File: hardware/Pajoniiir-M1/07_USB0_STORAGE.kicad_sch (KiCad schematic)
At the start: 7 parts

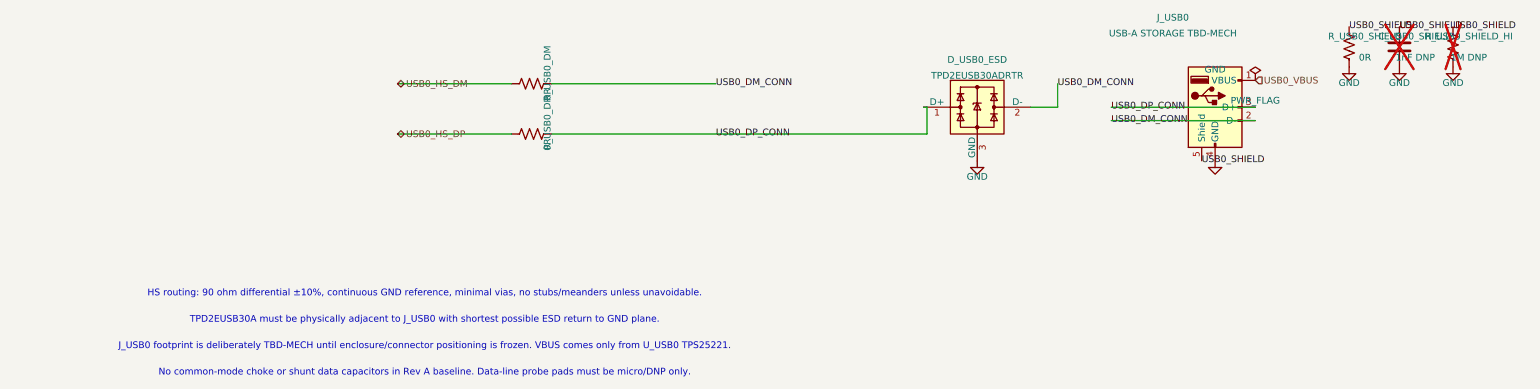
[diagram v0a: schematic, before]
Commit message: hardware: normalize schematic reference designators
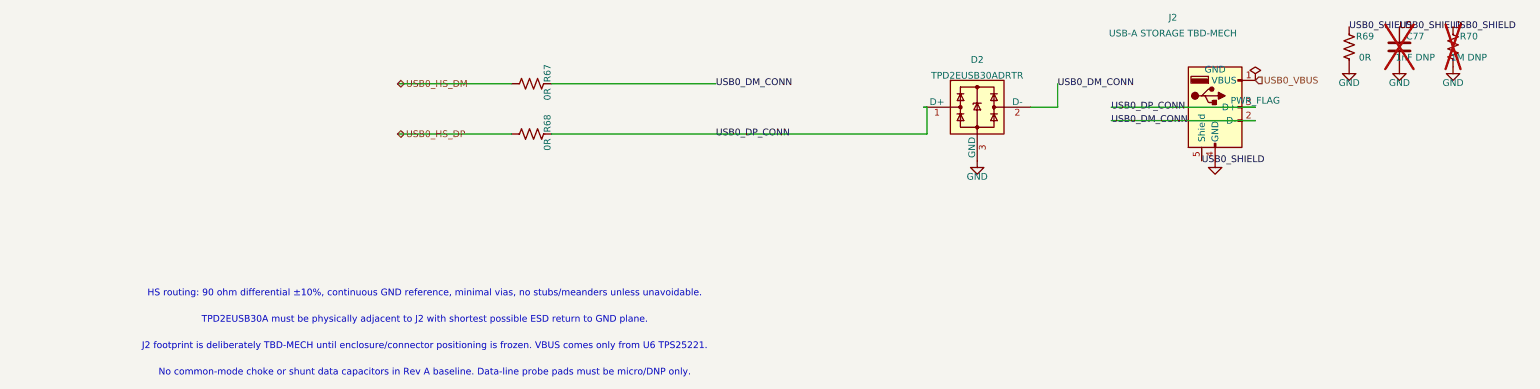
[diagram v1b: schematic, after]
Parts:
- renumbered C_USB0_SHIELD to C77, D_USB0_ESD to D2, J_USB0 to J2, R_USB0_DM to R67, R_USB0_DP to R68, R_USB0_SHIELD to R69, R_USB0_SHIELD_HI to R70
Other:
- note added: "J2 footprint is deliberately TBD-MECH until enclosure/connector positioning is frozen. VBUS comes only from U6 TPS25221."
- note added: "TPD2EUSB30A must be physically adjacent to J2 with shortest possible ESD return to GND plane."
- note removed: "J_USB0 footprint is deliberately TBD-MECH until enclosure/connector positioning is frozen. VBUS comes only from U_USB0 TPS25221."
- note removed: "TPD2EUSB30A must be physically adjacent to J_USB0 with shortest possible ESD return to GND plane."
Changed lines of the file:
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@@
     (lib_id "Device:R_US") (at 55.245 55.245 90) (unit 1)
     (exclude_from_sim no) (in_bom yes) (on_board yes) (dnp no)
-    (property "Reference" "R_USB0_DM" (at 58.245 53.245 0) (effects (font (size 1.27 1.27))))
+    (property "Reference" "R67" (at 58.245 53.245 0) (effects (font (size 1.27 1.27))))
     (property "Value" "0R" (at 58.245 57.245 0) (effects (font (size 1.27 1.27))))
     (property "Footprint" "Resistor_SMD:R_0402_1005Metric" (at 55.245 55.245 0) (effects (font (size 1.27 1.27)) (hide yes)))
     (property "Datasheet" "~" (at 55.245 55.245 0) (effects (font (size 1.27 1.27)) (hide yes)))
     (pin "1") (pin "2")
-    (instances (project "Pajoniiir-M1" (path "/2c8dd352-b7b8-4d9e-8f93-5dd43be2a100/31000007-6b2a-4a3a-8c91-000000000007" (reference "R_USB0_DM") (unit 1))))
+    (instances (project "Pajoniiir-M1" (path "/2c8dd352-b7b8-4d9e-8f93-5dd43be2a100/31000007-6b2a-4a3a-8c91-000000000007" (reference "R67") (unit 1))))
   )
   (wire (pts (xy 29.845 55.245) (xy 51.435 55.245)) (stroke (width 0) (type default)))
@@
     (lib_id "Device:R_US") (at 55.245 64.77 90) (unit 1)
     (exclude_from_sim no) (in_bom yes) (on_board yes) (dnp no)
-    (property "Reference" "R_USB0_DP" (at 58.245 62.77 0) (effects (font (size 1.27 1.27))))
+    (property "Reference" "R68" (at 58.245 62.77 0) (effects (font (size 1.27 1.27))))
     (property "Value" "0R" (at 58.245 66.77 0) (effects (font (size 1.27 1.27))))
     (property "Footprint" "Resistor_SMD:R_0402_1005Metric" (at 55.245 64.77 0) (effects (font (size 1.27 1.27)) (hide yes)))
     (property "Datasheet" "~" (at 55.245 64.77 0) (effects (font (size 1.27 1.27)) (hide yes)))
     (pin "1") (pin "2")
-    (instances (project "Pajoniiir-M1" (path "/2c8dd352-b7b8-4d9e-8f93-5dd43be2a100/31000007-6b2a-4a3a-8c91-000000000007" (reference "R_USB0_DP") (unit 1))))
+    (instances (project "Pajoniiir-M1" (path "/2c8dd352-b7b8-4d9e-8f93-5dd43be2a100/31000007-6b2a-4a3a-8c91-000000000007" (reference "R68") (unit 1))))
   )
   (wire (pts (xy 29.845 64.77) (xy 51.435 64.77)) (stroke (width 0) (type default)))
@@
     (lib_id "Power_Protection:TPD2EUSB30A") (at 139.7 59.69 0) (unit 1)
     (exclude_from_sim no) (in_bom yes) (on_board yes) (dnp no)
-    (property "Reference" "D_USB0_ESD" (at 139.7 50.69 0) (effects (font (size 1.27 1.27))))
+    (property "Reference" "D2" (at 139.7 50.69 0) (effects (font (size 1.27 1.27))))
     (property "Value" "TPD2EUSB30ADRTR" (at 139.7 53.69 0) (effects (font (size 1.27 1.27))))
     (property "Footprint" "Package_TO_SOT_SMD:Texas_DRT-3" (at 139.7 59.69 0) (effects (font (size 1.27 1.27)) (hide yes)))
     (property "Datasheet" "https://www.ti.com/lit/ds/symlink/tpd2eusb30a.pdf" (at 139.7 59.69 0) (effects (font (size 1.27 1.27)) (hide yes)))
     (pin "1") (pin "2") (pin "3")
-    (instances (project "Pajoniiir-M1" (path "/2c8dd352-b7b8-4d9e-8f93-5dd43be2a100/31000007-6b2a-4a3a-8c91-000000000007" (reference "D_USB0_ESD") (unit 1))))
+    (instances (project "Pajoniiir-M1" (path "/2c8dd352-b7b8-4d9e-8f93-5dd43be2a100/31000007-6b2a-4a3a-8c91-000000000007" (reference "D2") (unit 1))))
   )
   (wire (pts (xy 130.175 64.77) (xy 130.175 59.69)) (stroke (width 0) (type default)))
@@
     (lib_id "Connector:USB_A") (at 184.785 59.69 0) (unit 1)
     (exclude_from_sim no) (in_bom yes) (on_board yes) (dnp no)
-    (property "Reference" "J_USB0" (at 176.785 42.69 0) (effects (font (size 1.27 1.27))))
+    (property "Reference" "J2" (at 176.785 42.69 0) (effects (font (size 1.27 1.27))))
     (property "Value" "USB-A STORAGE TBD-MECH" (at 176.785 45.69 0) (effects (font (size 1.27 1.27))))
     (property "Footprint" "" (at 184.785 59.69 0) (effects (font (size 1.27 1.27)) (hide yes)))
     (property "Datasheet" "~" (at 184.785 59.69 0) (effects (font (size 1.27 1.27)) (hide yes)))
     (pin "1") (pin "2") (pin "3") (pin "4") (pin "5")
-    (instances (project "Pajoniiir-M1" (path "/2c8dd352-b7b8-4d9e-8f93-5dd43be2a100/31000007-6b2a-4a3a-8c91-000000000007" (reference "J_USB0") (unit 1))))
+    (instances (project "Pajoniiir-M1" (path "/2c8dd352-b7b8-4d9e-8f93-5dd43be2a100/31000007-6b2a-4a3a-8c91-000000000007" (reference "J2") (unit 1))))
   )
   (hierarchical_label "USB0_VBUS" (shape input) (at 192.405 54.61 0) (effects (font (size 1.27 1.27))))
@@
     (lib_id "Device:R_US") (at 210.185 48.26 0) (unit 1)
     (exclude_from_sim no) (in_bom yes) (on_board yes) (dnp no)
-    (property "Reference" "R_USB0_SHIELD" (at 213.185 46.26 0) (effects (font (size 1.27 1.27))))
+    (property "Reference" "R69" (at 213.185 46.26 0) (effects (font (size 1.27 1.27))))
     (property "Value" "0R" (at 213.185 50.26 0) (effects (font (size 1.27 1.27))))
     (property "Footprint" "Resistor_SMD:R_0603_1608Metric" (at 210.185 48.26 0) (effects (font (size 1.27 1.27)) (hide yes)))
     (property "Datasheet" "~" (at 210.185 48.26 0) (effects (font (size 1.27 1.27)) (hide yes)))
     (pin "1") (pin "2")
-    (instances (project "Pajoniiir-M1" (path "/2c8dd352-b7b8-4d9e-8f93-5dd43be2a100/31000007-6b2a-4a3a-8c91-000000000007" (reference "R_USB0_SHIELD") (unit 1))))
+    (instances (project "Pajoniiir-M1" (path "/2c8dd352-b7b8-4d9e-8f93-5dd43be2a100/31000007-6b2a-4a3a-8c91-000000000007" (reference "R69") (unit 1))))
   )
   (label "USB0_SHIELD" (at 210.185 44.45 0) (effects (font (size 1.27 1.27))))
@@
     (lib_id "Device:C") (at 219.71 48.26 0) (unit 1)
     (exclude_from_sim no) (in_bom yes) (on_board yes) (dnp yes)
-    (property "Reference" "C_USB0_SHIELD" (at 222.71 46.26 0) (effects (font (size 1.27 1.27))))
+    (property "Reference" "C77" (at 222.71 46.26 0) (effects (font (size 1.27 1.27))))
     (property "Value" "1nF DNP" (at 222.71 50.26 0) (effects (font (size 1.27 1.27))))
     (property "Footprint" "Capacitor_SMD:C_0603_1608Metric" (at 219.71 48.26 0) (effects (font (size 1.27 1.27)) (hide yes)))
     (property "Datasheet" "~" (at 219.71 48.26 0) (effects (font (size 1.27 1.27)) (hide yes)))
     (pin "1") (pin "2")
-    (instances (project "Pajoniiir-M1" (path "/2c8dd352-b7b8-4d9e-8f93-5dd43be2a100/31000007-6b2a-4a3a-8c91-000000000007" (reference "C_USB0_SHIELD") (unit 1))))
+    (instances (project "Pajoniiir-M1" (path "/2c8dd352-b7b8-4d9e-8f93-5dd43be2a100/31000007-6b2a-4a3a-8c91-000000000007" (reference "C77") (unit 1))))
   )
   (label "USB0_SHIELD" (at 219.71 44.45 0) (effects (font (size 1.27 1.27))))
@@
     (lib_id "Device:R_US") (at 229.87 48.26 0) (unit 1)
     (exclude_from_sim no) (in_bom yes) (on_board yes) (dnp yes)
-    (property "Reference" "R_USB0_SHIELD_HI" (at 232.87 46.26 0) (effects (font (size 1.27 1.27))))
+    (property "Reference" "R70" (at 232.87 46.26 0) (effects (font (size 1.27 1.27))))
     (property "Value" "1M DNP" (at 232.87 50.26 0) (effects (font (size 1.27 1.27))))
     (property "Footprint" "Resistor_SMD:R_0603_1608Metric" (at 229.87 48.26 0) (effects (font (size 1.27 1.27)) (hide yes)))
     (property "Datasheet" "~" (at 229.87 48.26 0) (effects (font (size 1.27 1.27)) (hide yes)))
     (pin "1") (pin "2")
-    (instances (project "Pajoniiir-M1" (path "/2c8dd352-b7b8-4d9e-8f93-5dd43be2a100/31000007-6b2a-4a3a-8c91-000000000007" (reference "R_USB0_SHIELD_HI") (unit 1))))
+    (instances (project "Pajoniiir-M1" (path "/2c8dd352-b7b8-4d9e-8f93-5dd43be2a100/31000007-6b2a-4a3a-8c91-000000000007" (reference "R70") (unit 1))))
   )
   (label "USB0_SHIELD" (at 229.87 44.45 0) (effects (font (size 1.27 1.27))))
@@
   )
   (text "HS routing: 90 ohm differential ±10%, continuous GND reference, minimal vias, no stubs/meanders unless unavoidable." (exclude_from_sim no) (at 35 95 0) (effects (font (size 1.27 1.27))))
-  (text "TPD2EUSB30A must be physically adjacent to J_USB0 with shortest possible ESD return to GND plane." (exclude_from_sim no) (at 35 100 0) (effects (font (size 1.27 1.27))))
-  (text "J_USB0 footprint is deliberately TBD-MECH until enclosure/connector positioning is frozen. VBUS comes only from U_USB0 TPS25221." (exclude_from_sim no) (at 35 105 0) (effects (font (size 1.27 1.27))))
+  (text "TPD2EUSB30A must be physically adjacent to J2 with shortest possible ESD return to GND plane." (exclude_from_sim no) (at 35 100 0) (effects (font (size 1.27 1.27))))
+  (text "J2 footprint is deliberately TBD-MECH until enclosure/connector positioning is frozen. VBUS comes only from U6 TPS25221." (exclude_from_sim no) (at 35 105 0) (effects (font (size 1.27 1.27))))
   (text "No common-mode choke or shunt data capacitors in Rev A baseline. Data-line probe pads must be micro/DNP only." (exclude_from_sim no) (at 35 110 0) (effects (font (size 1.27 1.27))))
   (symbol

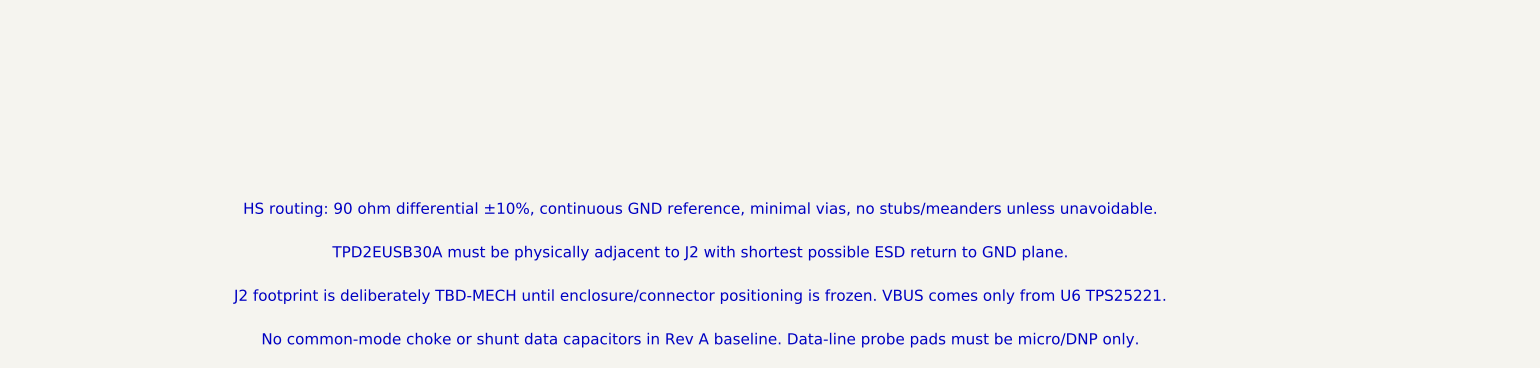
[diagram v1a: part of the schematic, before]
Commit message: hardware: constrain RefDes migration to annotation fields
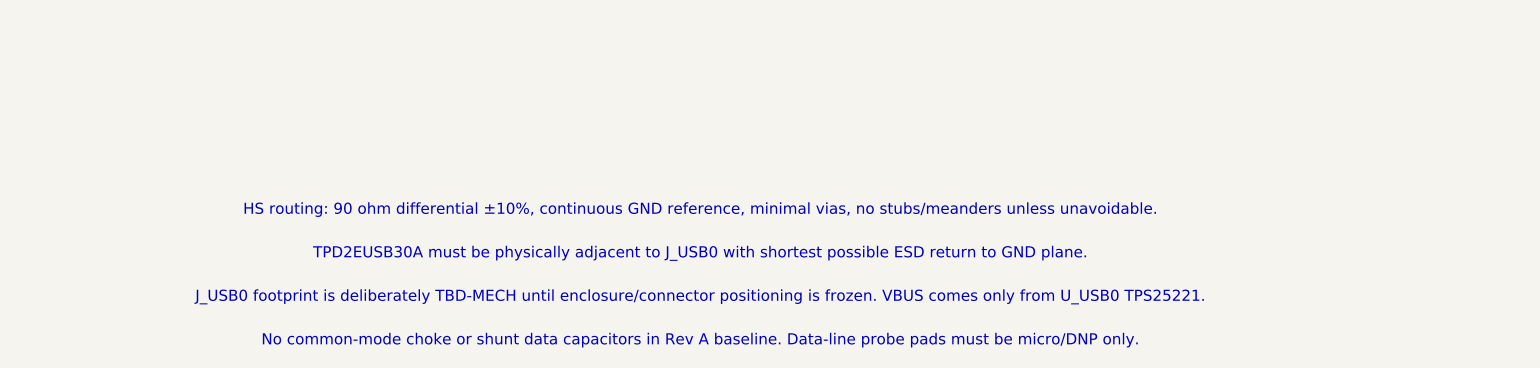
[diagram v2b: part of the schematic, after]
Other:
- note added: "J_USB0 footprint is deliberately TBD-MECH until enclosure/connector positioning is frozen. VBUS comes only from U_USB0 TPS25221."
- note added: "TPD2EUSB30A must be physically adjacent to J_USB0 with shortest possible ESD return to GND plane."
- note removed: "J2 footprint is deliberately TBD-MECH until enclosure/connector positioning is frozen. VBUS comes only from U6 TPS25221."
- note removed: "TPD2EUSB30A must be physically adjacent to J2 with shortest possible ESD return to GND plane."
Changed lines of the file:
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@@
   )
   (text "HS routing: 90 ohm differential ±10%, continuous GND reference, minimal vias, no stubs/meanders unless unavoidable." (exclude_from_sim no) (at 35 95 0) (effects (font (size 1.27 1.27))))
-  (text "TPD2EUSB30A must be physically adjacent to J2 with shortest possible ESD return to GND plane." (exclude_from_sim no) (at 35 100 0) (effects (font (size 1.27 1.27))))
-  (text "J2 footprint is deliberately TBD-MECH until enclosure/connector positioning is frozen. VBUS comes only from U6 TPS25221." (exclude_from_sim no) (at 35 105 0) (effects (font (size 1.27 1.27))))
+  (text "TPD2EUSB30A must be physically adjacent to J_USB0 with shortest possible ESD return to GND plane." (exclude_from_sim no) (at 35 100 0) (effects (font (size 1.27 1.27))))
+  (text "J_USB0 footprint is deliberately TBD-MECH until enclosure/connector positioning is frozen. VBUS comes only from U_USB0 TPS25221." (exclude_from_sim no) (at 35 105 0) (effects (font (size 1.27 1.27))))
   (text "No common-mode choke or shunt data capacitors in Rev A baseline. Data-line probe pads must be micro/DNP only." (exclude_from_sim no) (at 35 110 0) (effects (font (size 1.27 1.27))))
   (symbol
